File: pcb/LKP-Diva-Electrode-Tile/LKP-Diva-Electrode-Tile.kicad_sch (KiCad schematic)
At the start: 19 parts, among them J1 Intercon, J10 Electrode 0, J11 Electrode 2, J12 Electrode 4, J13 Electrode 6, J14 Electrode 8, J15 Electrode 10, J16 Electrode 12, J17 Electrode 14, J2 Electrode 1, J3 Electrode 3, J4 Electrode 5, J5 Electrode 7, J6 Electrode 9, J7 Electrode 11, J8 Electrode 13, J9 Electrode 15

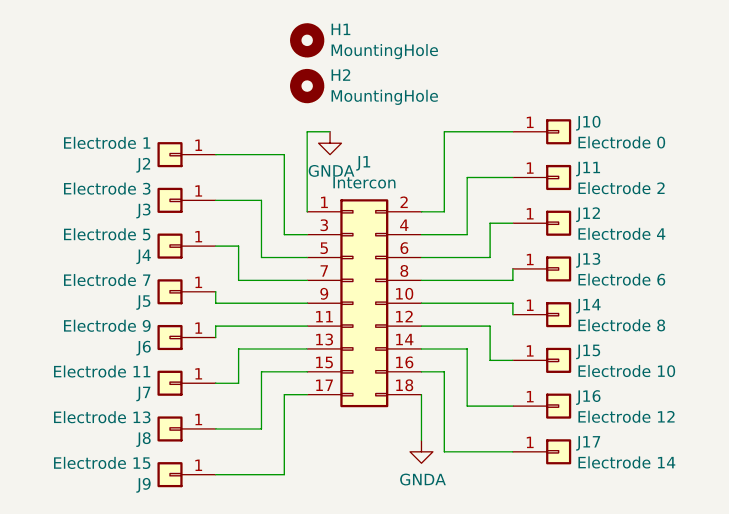
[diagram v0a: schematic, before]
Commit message: Update all active projects to KiCad 6.
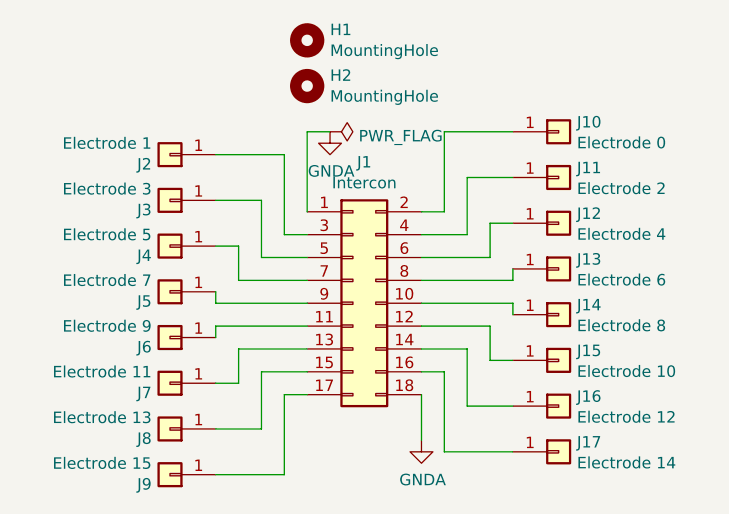
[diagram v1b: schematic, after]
